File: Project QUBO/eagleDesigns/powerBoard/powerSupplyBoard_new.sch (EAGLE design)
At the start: 146 parts

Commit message: placed everything preliminarily
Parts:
- C15, C3, C6: value (none) -> 22 uF
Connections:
- removed net N$59 (its old number): REN_B.1, REN_H.1, REN_T.2, U$5.C
- removed net N$60: R36.1, R37.2
- removed net N$61: ADC.SCL
- removed net N$63: ADC.SDA
- removed net N$75: BAT1HSOR.SHDN', HIGHSIDEMOS1.D, R48.1
- removed net N$76: ADC.CH7, R34.1, R35.2, R38.2
- removed net N$77: ADC.CH8
- removed net N$78: ADC.CH9
- removed net N$79: ADC.CH10
- removed net N$80: ADC.CH11
- removed net N$81: ADC.CH12
- removed net N$82: ADC.CH13
- removed net N$84: IOEXPANDER.SDA
- removed net N$86: IOEXPANDER.SCL
- new net N$32: ADC.CH7, R34.1, R35.2
- new net N$55: ADC.CH8, R36.1, R37.2
- net 12V: now also R42.2
- net 16V: now also R40.2
- net 3.3V: now also R46.2
- net 5V: now also R44.2
- net BAT2: now also R18.2
- net BAT3: now also R29.2, R38.2
- net GND: now also BAT1HSOR.SHDN', HIGHSIDEMOS1.D, R48.1, REN_B.1, REN_H.1, REN_T.2, U$5.C
- net N$66: now also ADC.CH9
- net N$71: now also ADC.CH10
- net N$72: now also ADC.CH11
- net N$73: now also ADC.CH12
- net N$74: now also ADC.CH13
- net SCL1: now also ADC.SCL, IOEXPANDER.SCL
- net SDA1: now also ADC.SDA, IOEXPANDER.SDA
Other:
- moved on the sheet: ADC, C13, C2, C5, JP1, R18, R29

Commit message: 
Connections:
- net N$24 renamed BAT2HSOROUT
- net N$39 renamed BAT1HSOROUT
- net N$41 renamed BAT3HSOROUT
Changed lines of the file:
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@@
 </segment>
 </net>
-<net name="N$39" class="0">
+<net name="BAT1HSOROUT" class="0">
 <segment>
 <pinref part="RSNS" gate="G$1" pin="2"/>
@@
 </segment>
 </net>
-<net name="N$24" class="0">
+<net name="BAT2HSOROUT" class="0">
 <segment>
 <pinref part="RSNS1" gate="G$1" pin="2"/>
@@
 </segment>
 </net>
-<net name="N$41" class="0">
+<net name="BAT3HSOROUT" class="0">
 <segment>
 <pinref part="RSNS2" gate="G$1" pin="2"/>

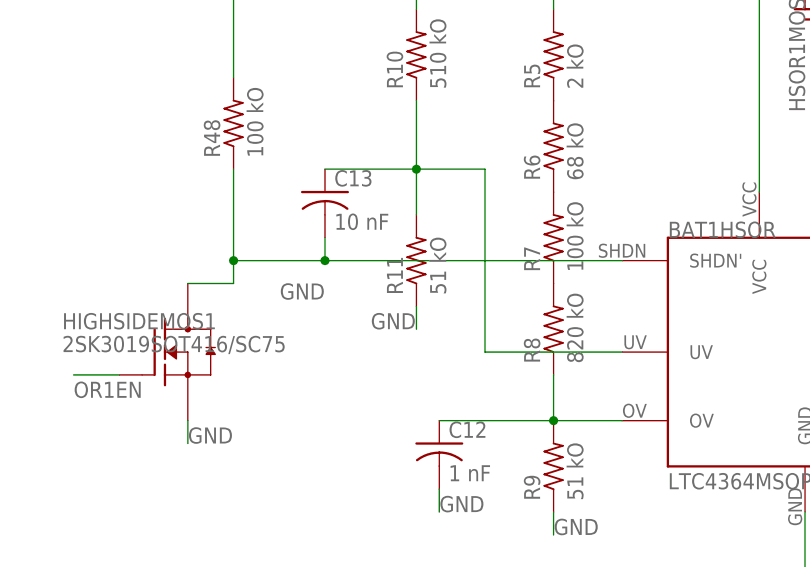
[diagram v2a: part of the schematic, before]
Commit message: 
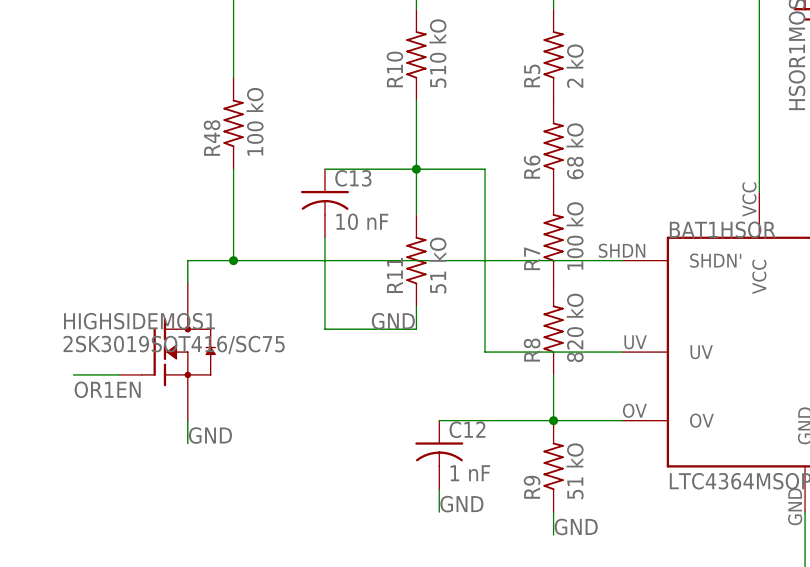
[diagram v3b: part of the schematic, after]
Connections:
- new net N$24: BAT1HSOR.SHDN', HIGHSIDEMOS1.D, R48.1
- net GND: no longer BAT1HSOR.SHDN', HIGHSIDEMOS1.D, R48.1
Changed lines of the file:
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@@
 <wire x1="-220.98" y1="96.52" x2="-220.98" y2="93.98" width="0.1524" layer="91"/>
 <label x="-226.06" y="93.98" size="1.778" layer="95"/>
+<pinref part="C13" gate="G$1" pin="2"/>
+<wire x1="-231.14" y1="104.14" x2="-231.14" y2="93.98" width="0.1524" layer="91"/>
+<wire x1="-231.14" y1="93.98" x2="-220.98" y2="93.98" width="0.1524" layer="91"/>
 </segment>
 <segment>
@@
 <label x="88.9" y="-93.98" size="1.778" layer="95"/>
 </segment>
-<segment>
-<pinref part="HIGHSIDEMOS1" gate="G$1" pin="D"/>
-<wire x1="-246.38" y1="99.06" x2="-241.3" y2="99.06" width="0.1524" layer="91"/>
-<wire x1="-241.3" y1="99.06" x2="-241.3" y2="101.6" width="0.1524" layer="91"/>
-<pinref part="R48" gate="G$1" pin="1"/>
-<pinref part="BAT1HSOR" gate="G$1" pin="SHDN'"/>
-<wire x1="-241.3" y1="101.6" x2="-241.3" y2="111.76" width="0.1524" layer="91"/>
-<wire x1="-198.12" y1="101.6" x2="-231.14" y2="101.6" width="0.1524" layer="91"/>
-<junction x="-241.3" y="101.6"/>
-<pinref part="C13" gate="G$1" pin="2"/>
-<wire x1="-231.14" y1="101.6" x2="-241.3" y2="101.6" width="0.1524" layer="91"/>
-<wire x1="-231.14" y1="104.14" x2="-231.14" y2="101.6" width="0.1524" layer="91"/>
-<junction x="-231.14" y="101.6"/>
-<label x="-231.14" y="99.06" size="1.778" layer="95" rot="R180"/>
-</segment>
 </net>
 <net name="N$9" class="0">
@@
 </segment>
 </net>
+<net name="N$24" class="0">
+<segment>
+<pinref part="BAT1HSOR" gate="G$1" pin="SHDN'"/>
+<pinref part="R48" gate="G$1" pin="1"/>
+<wire x1="-198.12" y1="101.6" x2="-241.3" y2="101.6" width="0.1524" layer="91"/>
+<wire x1="-241.3" y1="101.6" x2="-241.3" y2="111.76" width="0.1524" layer="91"/>
+<pinref part="HIGHSIDEMOS1" gate="G$1" pin="D"/>
+<wire x1="-241.3" y1="101.6" x2="-246.38" y2="101.6" width="0.1524" layer="91"/>
+<wire x1="-246.38" y1="101.6" x2="-246.38" y2="99.06" width="0.1524" layer="91"/>
+<junction x="-241.3" y="101.6"/>
+</segment>
+</net>

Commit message: psb layout updates
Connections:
- new net N$24: C13.2, R11.1
- net GND: no longer C13.2, R11.1
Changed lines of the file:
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@@
-</segment>
-<segment>
-<pinref part="R11" gate="G$1" pin="1"/>
-<wire x1="-220.98" y1="96.52" x2="-220.98" y2="93.98" width="0.1524" layer="91"/>
-<label x="-226.06" y="93.98" size="1.778" layer="95"/>
-<pinref part="C13" gate="G$1" pin="2"/>
-<wire x1="-231.14" y1="104.14" x2="-231.14" y2="93.98" width="0.1524" layer="91"/>
-<wire x1="-231.14" y1="93.98" x2="-220.98" y2="93.98" width="0.1524" layer="91"/>
 </segment>
 <segment>
@@
 <wire x1="-241.3" y1="-7.62" x2="-241.3" y2="-5.08" width="0.1524" layer="91"/>
 <wire x1="-241.3" y1="-5.08" x2="-198.12" y2="-5.08" width="0.1524" layer="91"/>
+<junction x="-241.3" y="-5.08"/>
 </segment>
 </net>
 <net name="N$24" class="0">
 <segment>
+<pinref part="C13" gate="G$1" pin="2"/>
+<wire x1="-231.14" y1="104.14" x2="-231.14" y2="93.98" width="0.1524" layer="91"/>
+<wire x1="-231.14" y1="93.98" x2="-220.98" y2="93.98" width="0.1524" layer="91"/>
+<pinref part="R11" gate="G$1" pin="1"/>
+<wire x1="-220.98" y1="96.52" x2="-220.98" y2="93.98" width="0.1524" layer="91"/>
+<label x="-226.06" y="93.98" size="1.778" layer="95"/>
+</segment>
+</net>
+<net name="N$39" class="0">
+<segment>
+<pinref part="R48" gate="G$1" pin="1"/>
+<wire x1="-241.3" y1="111.76" x2="-241.3" y2="101.6" width="0.1524" layer="91"/>
+<pinref part="HIGHSIDEMOS1" gate="G$1" pin="D"/>
+<wire x1="-241.3" y1="101.6" x2="-241.3" y2="99.06" width="0.1524" layer="91"/>
+<wire x1="-241.3" y1="99.06" x2="-246.38" y2="99.06" width="0.1524" layer="91"/>
 <pinref part="BAT1HSOR" gate="G$1" pin="SHDN'"/>
-<pinref part="R48" gate="G$1" pin="1"/>
 <wire x1="-198.12" y1="101.6" x2="-241.3" y2="101.6" width="0.1524" layer="91"/>
-<wire x1="-241.3" y1="101.6" x2="-241.3" y2="111.76" width="0.1524" layer="91"/>
-<pinref part="HIGHSIDEMOS1" gate="G$1" pin="D"/>
-<wire x1="-241.3" y1="101.6" x2="-246.38" y2="101.6" width="0.1524" layer="91"/>
-<wire x1="-246.38" y1="101.6" x2="-246.38" y2="99.06" width="0.1524" layer="91"/>
 <junction x="-241.3" y="101.6"/>
 </segment>

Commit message: 
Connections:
- new net UWEEN: DVL_12VREG.ON/OFFCTRL, IOEXPANDER.P05
- net BAT1: now also BAT1.P$2
- net BAT2: now also BAT2.P$2
- net BAT3: now also SHORE.P$2
- net GND: no longer BAT1.P$2, BAT2.P$2, SHORE.P$2
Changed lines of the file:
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@@
 <layer number="2" name="Route2" color="1" fill="3" visible="no" active="no"/>
 <layer number="3" name="Route3" color="4" fill="3" visible="no" active="no"/>
+<layer number="4" name="Route4" color="1" fill="4" visible="no" active="no"/>
+<layer number="5" name="Route5" color="4" fill="4" visible="no" active="no"/>
+<layer number="6" name="Route6" color="1" fill="8" visible="no" active="no"/>
+<layer number="7" name="Route7" color="4" fill="8" visible="no" active="no"/>
+<layer number="8" name="Route8" color="1" fill="2" visible="no" active="no"/>
+<layer number="9" name="Route9" color="4" fill="2" visible="no" active="no"/>
+<layer number="10" name="Route10" color="1" fill="7" visible="no" active="no"/>
+<layer number="11" name="Route11" color="4" fill="7" visible="no" active="no"/>
+<layer number="12" name="Route12" color="1" fill="5" visible="no" active="no"/>
+<layer number="13" name="Route13" color="4" fill="5" visible="no" active="no"/>
 <layer number="14" name="Route14" color="1" fill="6" visible="no" active="no"/>
 <layer number="15" name="Route15" color="4" fill="6" visible="no" active="no"/>
@@
 <label x="104.14" y="-205.74" size="1.778" layer="95"/>
 </segment>
+<segment>
+<pinref part="BAT1" gate="G$1" pin="P$2"/>
+<wire x1="-297.18" y1="20.32" x2="-289.56" y2="20.32" width="0.1524" layer="91"/>
+<label x="-294.64" y="20.32" size="1.778" layer="95"/>
+</segment>
 </net>
 <net name="BAT2" class="0">
@@
 <label x="93.98" y="-205.74" size="1.778" layer="95"/>
 </segment>
+<segment>
+<pinref part="BAT2" gate="G$1" pin="P$2"/>
+<wire x1="-297.18" y1="-5.08" x2="-289.56" y2="-5.08" width="0.1524" layer="91"/>
+<label x="-294.64" y="-5.08" size="1.778" layer="95"/>
+</segment>
 </net>
 <net name="GND" class="0">
@@
 <wire x1="-101.6" y1="119.38" x2="-101.6" y2="114.3" width="0.1524" layer="91"/>
 <label x="-101.6" y="114.3" size="1.778" layer="95"/>
-</segment>
-<segment>
-<pinref part="BAT1" gate="G$1" pin="P$2"/>
-<wire x1="-297.18" y1="20.32" x2="-289.56" y2="20.32" width="0.1524" layer="91"/>
-<label x="-294.64" y="20.32" size="1.778" layer="95"/>
-</segment>
-<segment>
-<pinref part="BAT2" gate="G$1" pin="P$2"/>
-<wire x1="-297.18" y1="-5.08" x2="-289.56" y2="-5.08" width="0.1524" layer="91"/>
-<label x="-294.64" y="-5.08" size="1.778" layer="95"/>
-</segment>
-<segment>
-<pinref part="SHORE" gate="G$1" pin="P$2"/>
-<wire x1="-297.18" y1="-30.48" x2="-289.56" y2="-30.48" width="0.1524" layer="91"/>
-<label x="-294.64" y="-30.48" size="1.778" layer="95"/>
 </segment>
 <segment>
@@
 <label x="83.82" y="-205.74" size="1.778" layer="95"/>
 </segment>
+<segment>
+<pinref part="SHORE" gate="G$1" pin="P$2"/>
+<wire x1="-297.18" y1="-30.48" x2="-289.56" y2="-30.48" width="0.1524" layer="91"/>
+<label x="-294.64" y="-30.48" size="1.778" layer="95"/>
+</segment>
 </net>
 <net name="N$46" class="0">
@@
 </segment>
 </net>
+<net name="UWEEN" class="0">
+<segment>
+<pinref part="IOEXPANDER" gate="G$1" pin="P05"/>
+<wire x1="147.32" y1="-154.94" x2="142.24" y2="-154.94" width="0.1524" layer="91"/>
+<label x="137.16" y="-154.94" size="1.778" layer="95"/>
+</segment>
+<segment>
+<pinref part="DVL_12VREG" gate="G$1" pin="ON/OFFCTRL"/>
+<wire x1="50.8" y1="129.54" x2="40.64" y2="129.54" width="0.1524" layer="91"/>
+<label x="40.64" y="129.54" size="1.778" layer="95"/>
+</segment>
+</net>
